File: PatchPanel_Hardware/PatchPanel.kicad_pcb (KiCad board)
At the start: 2 copper layers, 148.6 x 101.6 mm, 103 parts, among them Q1 Q_PMOS_GDS, Q10 Q_PMOS_GDS, Q11 Q_NMOS_GSD, Q12 Q_NMOS_GSD, Q13 Q_PMOS_GDS, Q14 Q_PMOS_GDS, Q15 Q_NMOS_GSD, Q16 Q_NMOS_GSD, Q17 Q_PMOS_GDS, Q18 Q_PMOS_GDS, Q19 Q_NMOS_GSD, Q2 Q_PMOS_GDS, Q20 Q_NMOS_GSD, Q21 Q_PMOS_GDS, Q22 Q_PMOS_GDS, Q23 Q_NMOS_GSD, Q24 Q_NMOS_GSD, Q25 Q_PMOS_GDS, Q26 Q_PMOS_GDS, Q27 Q_NMOS_GSD, Q28 Q_NMOS_GSD, Q29 Q_PMOS_GDS, Q3 Q_NMOS_GSD, Q30 Q_PMOS_GDS, Q31 Q_NMOS_GSD, Q32 Q_NMOS_GSD, Q4 Q_NMOS_GSD, Q5 Q_PMOS_GDS, Q6 Q_PMOS_GDS, Q7 Q_NMOS_GSD, Q8 Q_NMOS_GSD, Q9 Q_PMOS_GDS

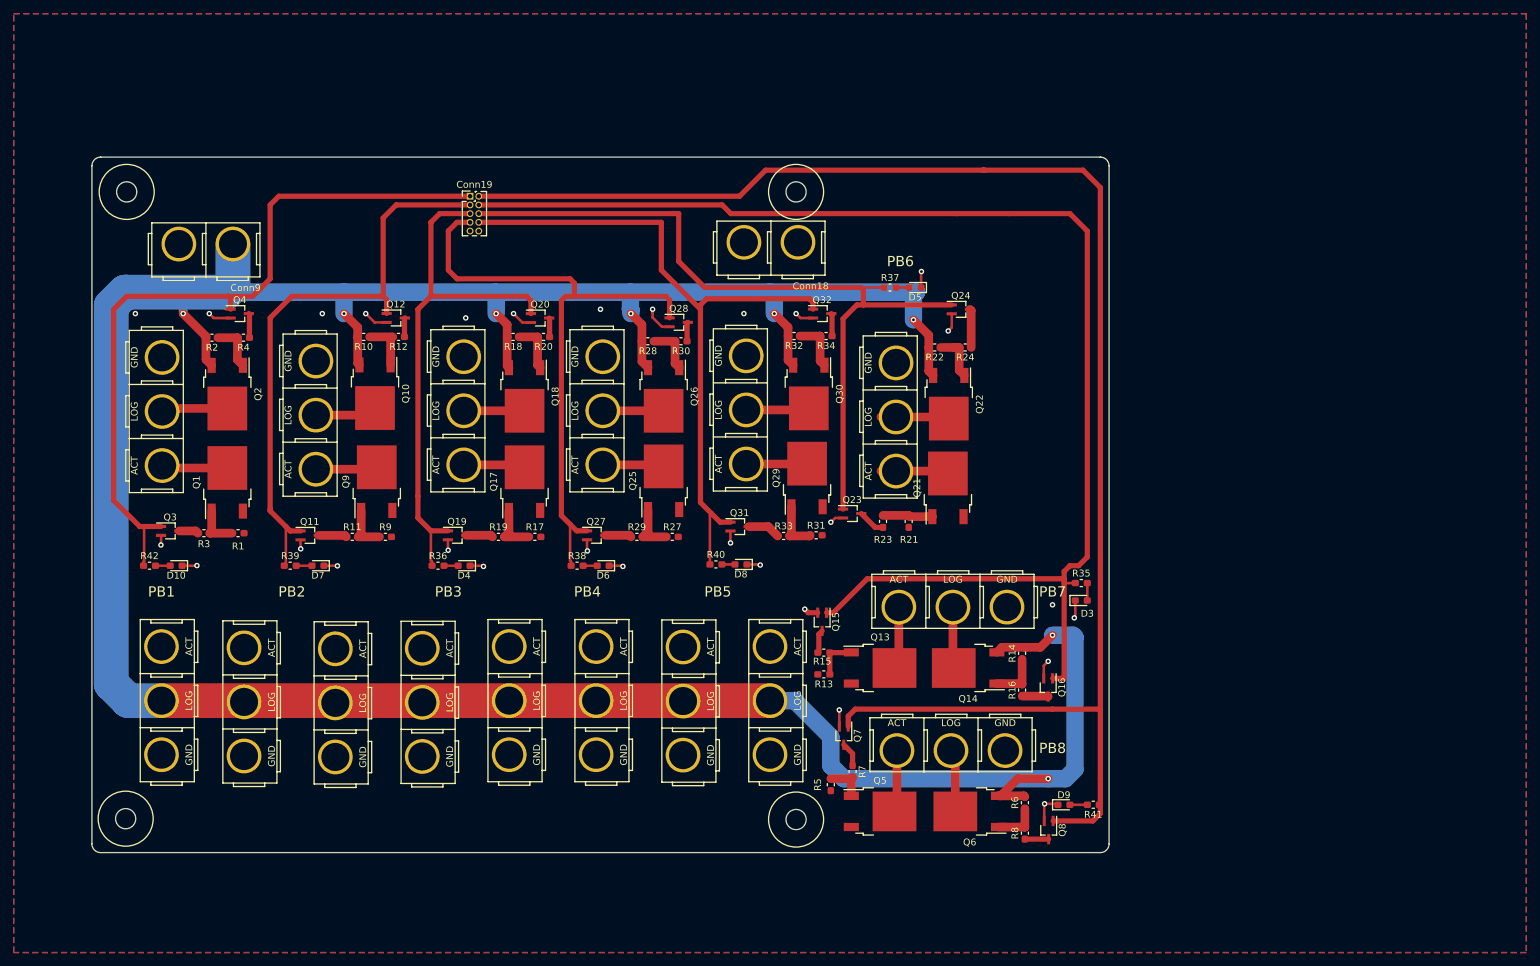
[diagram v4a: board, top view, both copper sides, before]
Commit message: Redid entire schematic to be more organized and compact
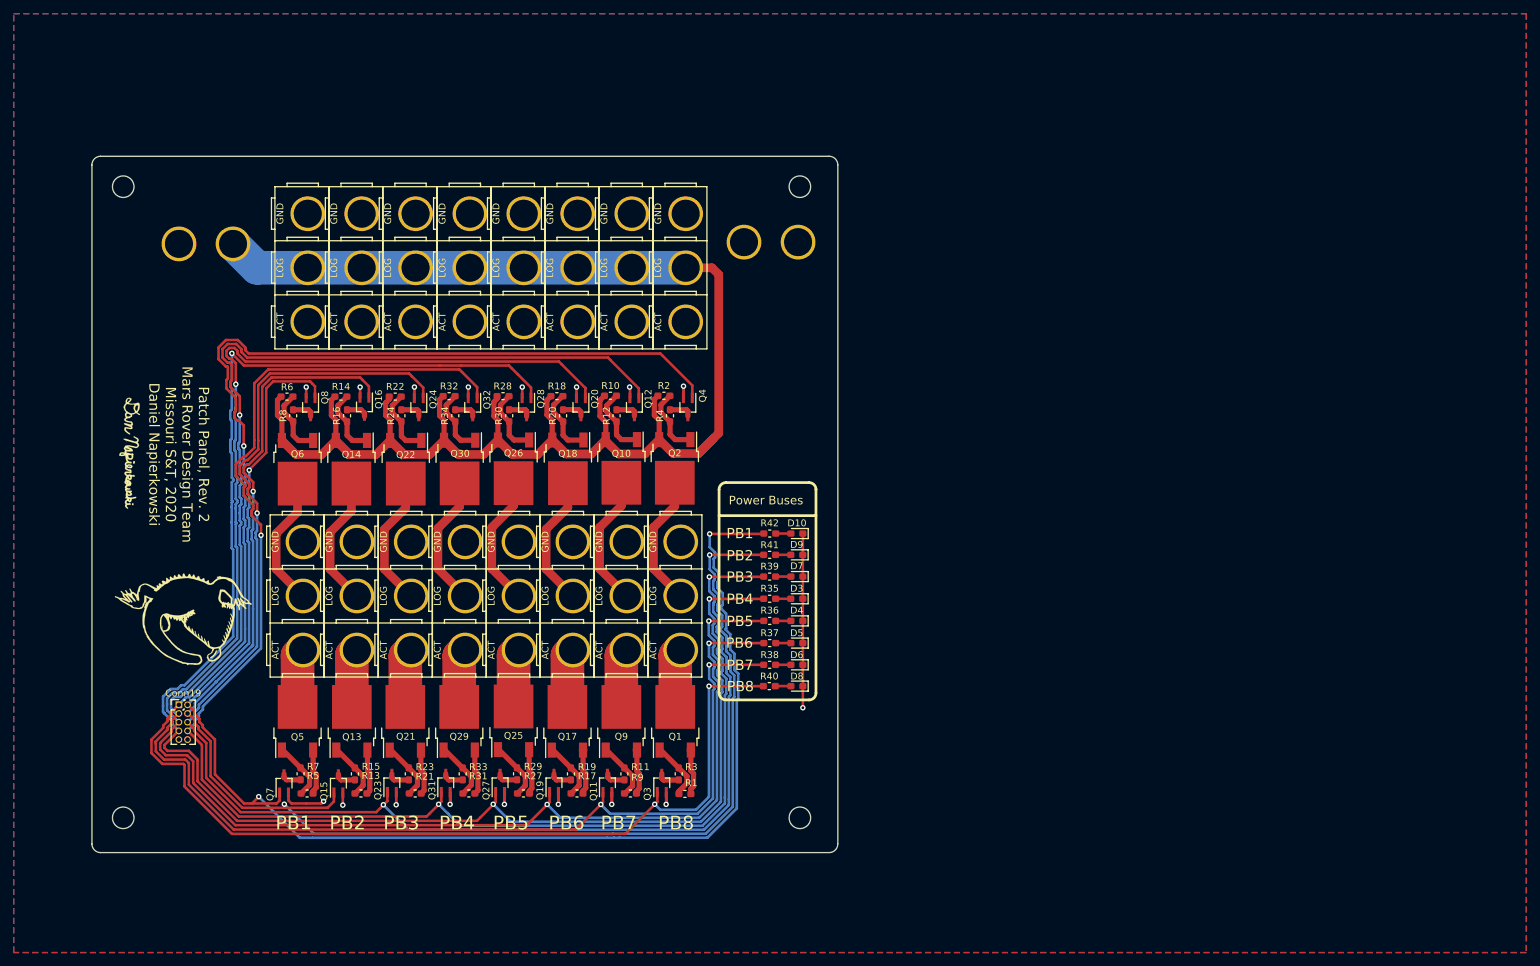
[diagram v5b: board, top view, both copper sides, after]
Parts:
- removed REF** (x4): 4_40_Hole, MRDT_Drill_Holes:4_40_Hole
- added G***: LOGO, ESP8266:Signature, F.Cu at (47.5, 88.9)
- added G***: LOGO, ESP8266:lizard_logo, F.Cu at (55.4, 114.8)
- Conn18, Conn9: moved to B.Cu
- moved Q8 124.3 mm to (73.9, 82.2)
- moved R8 123.1 mm to (71.3, 83.5), turned to 270 degrees
- moved R6 123.0 mm to (70.4, 80.7), turned to 180 degrees
- moved Conn11 116.2 mm to (68.6, 50.0), turned to 270 degrees
- moved Conn2 115.2 mm to (67.9, 98.0), turned to 270 degrees
- moved Q6 110.2 mm to (71.9, 91.3), turned to 270 degrees
- moved Conn15 109.7 mm to (123.9, 50.0), turned to 270 degrees
- moved Q16 108.0 mm to (81.7, 82.2)
- moved R16 106.5 mm to (79.2, 83.5), turned to 270 degrees
- moved R14 106.3 mm to (78.3, 80.7), turned to 180 degrees
- moved Conn4 104.1 mm to (75.8, 98.0), turned to 270 degrees
- moved Conn16 103.8 mm to (76.5, 50.0), turned to 270 degrees
- moved Conn17 99.0 mm to (116.0, 50.0), turned to 270 degrees
- moved Q14 94.7 mm to (79.8, 91.3), turned to 270 degrees
- moved Conn14 94.1 mm to (84.4, 50.0), turned to 270 degrees
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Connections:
- Conn19 pad 1: PB1 -> PB8
- Conn19 pad 2: PB2 -> PB1
- Conn19 pad 3: PB3 -> PB7
- Conn19 pad 4: PB4 -> PB2
- Conn19 pad 5: PB5 -> PB6
- Conn19 pad 6: PB6 -> PB3
- Conn19 pad 7: PB7 -> PB5
- Conn19 pad 8: PB8 -> PB4
- Q11 pad 1: PB3 -> PB7
- Q12 pad 1: PB3 -> PB7
- Q15 pad 1: PB4 -> PB2
- Q16 pad 1: PB4 -> PB2
- Q19 pad 1: PB5 -> PB6
- Q20 pad 1: PB5 -> PB6
- Q23 pad 1: PB6 -> PB3
- Q24 pad 1: PB6 -> PB3
- Q27 pad 1: PB7 -> PB5
- Q28 pad 1: PB7 -> PB5
- Q3 pad 1: PB1 -> PB8
- Q31 pad 1: PB8 -> PB4
- Q32 pad 1: PB8 -> PB4
- Q4 pad 1: PB1 -> PB8
- Q7 pad 1: PB2 -> PB1
- Q8 pad 1: PB2 -> PB1
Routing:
- net /Vlog: track 480.6 -> 232.5 mm, vias 8 -> 0
- net PB5: track 77.3 -> 241.3 mm, vias 0 -> 3
- net PB7: track 91.6 -> 254.7 mm, vias 0 -> 3
- net PB8: track 101.7 -> 259.6 mm, vias 0 -> 3
- net PB3: track 85.2 -> 219.8 mm, vias 0 -> 3
- net PB6: track 115.0 -> 248.7 mm, vias 0 -> 3
- net PB1: track 109.5 -> 211.7 mm, vias 0 -> 3
- net /Vact: track 0.55 -> 53.6 mm
- net PB4: track 198.1 -> 226.1 mm, vias 0 -> 3
- net GND: track 56.5 -> 69.8 mm, vias 29 -> 17
- net Net-(Conn3-Pad2): track 9.07 -> 21.0 mm
- net Net-(Conn7-Pad2): track 8.89 -> 19.4 mm
- net Net-(Conn5-Pad2): track 8.89 -> 19.4 mm
- net Net-(Conn4-Pad2): track 8.94 -> 19.3 mm
- net Net-(Conn2-Pad2): track 9.15 -> 19.3 mm
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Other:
- board size 148.6 x 101.6 mm -> 109 x 101.7 mm
- board text added: "Patch Panel, Rev. 2 Mars Rover Design Team Missouri S&T, 2020 Daniel Napierkowski"
- board text added: "Power Buses"

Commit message: added some silks, generated Gerbs
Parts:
- added G***: LOGO, MRDT_Silkscreens:0_MRDT_Logo_10mm, F.Cu at (143.0, 74.5)
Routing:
- net /Vlog: track 232.5 -> 241.4 mm, vias 0 -> 8
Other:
- board text added: "Always On"
